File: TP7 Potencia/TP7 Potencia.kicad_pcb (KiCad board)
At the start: 2 copper layers, 55 parts, among them J1 Input, Q1 IRF830PBF, Q2 IRF830PBF, Q3 IRF830PBF, Q4 IRF830PBF, Q5 BC337, Q6 BC337, Q7 2N7000, Q8 2N7000, SW1 SW_Push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

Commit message: Placement de componentes en el PCB
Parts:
- added D11: MUR160, MUR160:DIOAD1300W80L670D310, F.Cu at (225.7, 34.5)
- added D12: MUR160, MUR160:DIOAD1300W80L670D310, F.Cu at (236.2, 49.7)
- added D13: MUR160, MUR160:DIOAD1300W80L670D310, F.Cu at (153.5, 50.2)
- added D14: MUR160, MUR160:DIOAD1300W80L670D310, F.Cu at (147.2, 39.6)
- added J2: PWM, Connector_PinSocket_2.54mm:PinSocket_1x01_P2.54mm_Vertical, F.Cu at (55.6, 26.9)
- moved U6 171.0 mm to (255.6, 145.2)
- moved C10 160.3 mm to (236.4, 144.0)
- moved C8 160.3 mm to (236.4, 137.7)
- moved C9 160.3 mm to (236.4, 140.8)
- moved D7 160.3 mm to (242.2, 118.7)
- moved D8 160.3 mm to (242.2, 122.2)
- moved D9 160.3 mm to (242.2, 125.8)
- moved Q5 160.3 mm to (230.3, 129.9)
- moved Q6 160.3 mm to (230.3, 135.7)
- moved Q7 160.3 mm to (230.3, 141.5)
- moved Q8 160.3 mm to (230.3, 147.3)
- moved RV3 160.3 mm to (269.8, 117.9)
- moved RV4 160.3 mm to (269.8, 124.0)
- moved R10 160.3 mm to (208.6, 121.8)
- moved R11 160.3 mm to (208.6, 125.8)
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
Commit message: Ordenados los componentes por bloques
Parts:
- D11, D12, D13, D14, D2, D4: footprint MUR160:DIOAD1300W80L670D310 -> Diode_THT:D_DO-35_SOD27_P7.62mm_Horizontal
- moved RV3 153.4 mm to (120.2, 83.8), turned to 90 degrees
- moved RV4 124.6 mm to (148.7, 94.8), turned to 90 degrees
- moved D9 105.9 mm to (141.0, 94.4), turned to -90 degrees
- moved U5 104.5 mm to (128.6, 84.5)
- moved D12 101.7 mm to (134.5, 50.4), turned to -90 degrees
- moved U6 99.2 mm to (232.6, 48.6)
- moved D11 97.7 mm to (128.3, 42.6), turned to -90 degrees
- moved R10 93.7 mm to (119.7, 92.1), turned to -90 degrees
- moved C10 89.6 mm to (156.8, 102.9), turned to -90 degrees
- moved Q5 87.5 mm to (155.9, 83.8), turned to -90 degrees
- moved R9 87.5 mm to (125.0, 91.9), turned to -90 degrees
- moved Q7 85.2 mm to (156.9, 98.3), turned to 90 degrees
- moved C8 82.5 mm to (219.8, 56.9)
- moved R12 81.8 mm to (140.1, 85.1)
- moved Q8 81.1 mm to (173.5, 89.4), turned to 90 degrees
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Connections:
- C1 pad 1: Net-(U2-VB) -> Net-(D2-K)
- C4 pad 1: Net-(U2-VB) -> Net-(D2-K)
- C5 pad 1: Net-(U3-VB) -> Net-(D4-K)
- C6 pad 1: Net-(U3-VB) -> Net-(D4-K)
- D10 pad 2: Net-(D10-A) -> SD
- Q8 pad 1: Net-(D10-A) -> SD
- R16 pad 2: Net-(D10-A) -> SD
- U2 pad 6: Net-(U2-VB) -> Net-(D2-K)
- U3 pad 6: Net-(U3-VB) -> Net-(D4-K)

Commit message: Ruteo
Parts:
- Q6: moved to B.Cu
- moved D8 182.4 mm to (58.9, 56.4), turned to 0 degrees
- moved R8 179.2 mm to (67.2, 51.2), turned to 180 degrees
- moved C9 178.5 mm to (55.7, 56.4)
- moved U6 174.3 mm to (59.1, 64.9), turned to 90 degrees
- moved R7 171.1 mm to (51.4, 77.7), turned to 0 degrees
- moved D7 165.9 mm to (60.1, 73.2), turned to 180 degrees
- moved C8 153.9 mm to (67.3, 77.7), turned to 90 degrees
- moved C4 76.7 mm to (177.1, 39.7), turned to 180 degrees
- moved D1 74.6 mm to (185.2, 41.7)
- moved D2 74.6 mm to (179.3, 36.3)
- moved R3 74.6 mm to (183.9, 37.2)
- moved C1 74.6 mm to (186.1, 46.6)
- moved D11 74.6 mm to (202.9, 44.3)
- moved Q1 74.6 mm to (195.8, 48.6)
- moved U2 74.6 mm to (179.7, 59.3)
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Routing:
- net 12V: track 0.00 -> 205.3 mm
- net H1: track 0.00 -> 57.8 mm
- net H2: track 0.00 -> 54.4 mm
- net PWM: track 0.00 -> 45.0 mm
- net H: track 0.00 -> 36.4 mm
- net Net-(D4-K): track 0.00 -> 19.4 mm
- net 5V: track 0.00 -> 18.9 mm
- net Net-(D2-K): track 0.00 -> 18.7 mm
- net Net-(U1-DTC): track 0.00 -> 17.3 mm
- net B: track 0.00 -> 16.7 mm
- net Net-(D3-A): track 0.00 -> 14.7 mm
- net Net-(D6-A): track 0.00 -> 13.9 mm
- net Net-(D6-K): track 0.00 -> 12.9 mm
- net E: track 0.00 -> 12.7 mm
- net Net-(D3-K): track 0.00 -> 11.6 mm
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
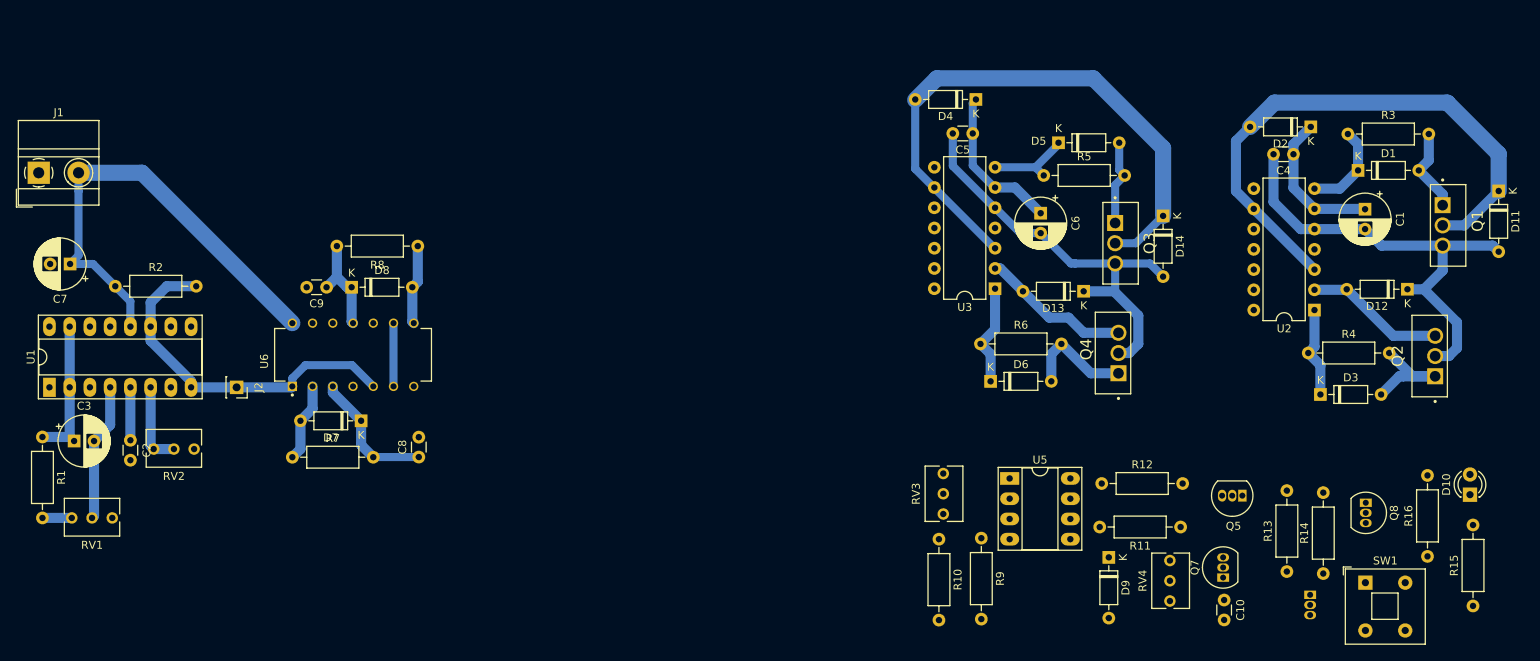
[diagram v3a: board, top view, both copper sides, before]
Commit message: continuacion del rooteo y agregado de testpoint y borneras
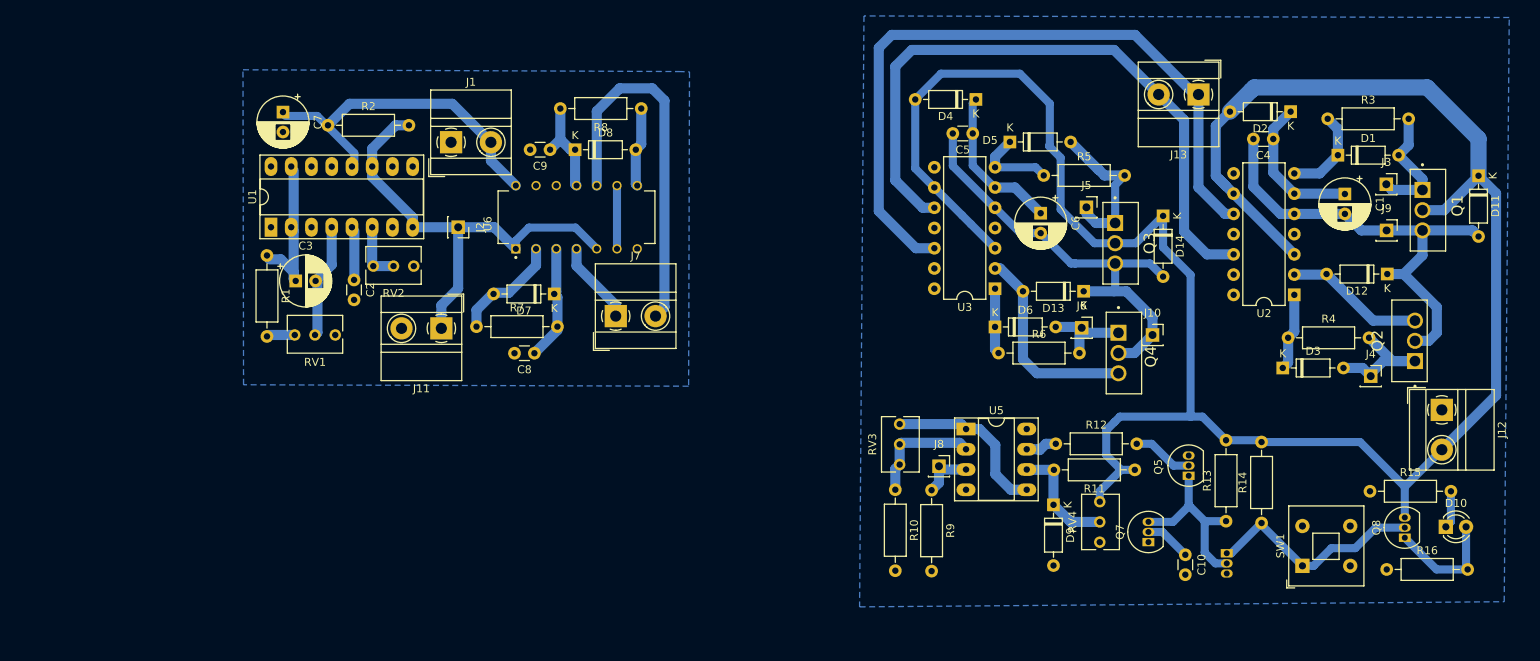
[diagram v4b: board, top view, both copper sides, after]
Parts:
- added J10: H2, Connector_PinSocket_2.54mm:PinSocket_1x01_P2.54mm_Vertical, F.Cu at (159.4, 62.4)
- added J11: GND/PWM, TerminalBlock_MetzConnect:TerminalBlock_MetzConnect_Type011_RT05502HBWC_1x02_P5.00mm_Horizontal, F.Cu at (70.1, 61.5)
- added J12: Input, TerminalBlock_MetzConnect:TerminalBlock_MetzConnect_Type011_RT05502HBWC_1x02_P5.00mm_Horizontal, F.Cu at (195.7, 71.8)
- added J13: PWM1/PWM2, TerminalBlock_MetzConnect:TerminalBlock_MetzConnect_Type011_RT05502HBWC_1x02_P5.00mm_Horizontal, F.Cu at (165.2, 32.2)
- added J3: Gate Q1, Connector_PinSocket_2.54mm:PinSocket_1x01_P2.54mm_Vertical, F.Cu at (188.8, 43.5)
- added J4: Gate Q2, Connector_PinSocket_2.54mm:PinSocket_1x01_P2.54mm_Vertical, F.Cu at (186.8, 67.5)
- added J5: Gate Q3, Connector_PinSocket_2.54mm:PinSocket_1x01_P2.54mm_Vertical, F.Cu at (151.1, 46.4)
- added J6: Gate Q4, Connector_PinSocket_2.54mm:PinSocket_1x01_P2.54mm_Vertical, F.Cu at (150.5, 61.5)
- added J7: Output, TerminalBlock_MetzConnect:TerminalBlock_MetzConnect_Type011_RT05502HBWC_1x02_P5.00mm_Horizontal, F.Cu at (92.0, 60.0)
- added J8: H, Connector_PinSocket_2.54mm:PinSocket_1x01_P2.54mm_Vertical, F.Cu at (132.6, 78.9)
- added J9: H1, Connector_PinSocket_2.54mm:PinSocket_1x01_P2.54mm_Vertical, F.Cu at (188.8, 49.3)
- moved J1 51.9 mm to (71.4, 38.2)
- moved R1 36.2 mm to (48.2, 52.4)
- moved RV1 36.2 mm to (51.7, 62.4)
- moved RV2 35.9 mm to (61.6, 53.7)
- moved C2 34.5 mm to (59.2, 55.5)
- moved C3 34.3 mm to (51.9, 55.6)
- moved J2 34.3 mm to (72.3, 48.9)
- moved U1 34.3 mm to (48.8, 48.9)
- moved R2 33.5 mm to (55.9, 36.1)
- moved C9 32.9 mm to (83.8, 39.1)
- moved D8 32.9 mm to (86.9, 39.1)
- moved R8 32.9 mm to (95.2, 34.0)
- moved U6 32.9 mm to (87.1, 47.6)
- moved C7 32.8 mm to (50.3, 34.4), turned to -90 degrees
- moved D7 29.0 mm to (84.3, 57.2)
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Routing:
- net PWM2: track 0.00 -> 130.0 mm
- net 12V: track 205.3 -> 317.9 mm
- net PWM1: track 0.00 -> 101.2 mm
- net Net-(Q6-C): track 0.00 -> 34.1 mm
- net Net-(Q5-C): track 0.00 -> 22.5 mm
- net Net-(U5B-+): track 0.00 -> 21.5 mm
- net SD: track 0.17 -> 15.0 mm
- net Net-(U5A--): track 0.00 -> 14.7 mm
- net Net-(D9-K): track 0.00 -> 14.5 mm
- net H: track 36.4 -> 50.5 mm
- net PWM: track 45.0 -> 58.4 mm
- net Net-(D5-A): track 10.9 -> 19.9 mm
- net Net-(Q5-B): track 0.00 -> 7.65 mm
- net Net-(D1-A): track 10.7 -> 15.5 mm
- net Net-(D7-A): track 9.94 -> 14.6 mm
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- added copper zone on B.Cu, net GND

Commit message: fin del rooteo
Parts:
- RV1: footprint Potentiometer_THT:Potentiometer_Bourns_3266Y_Vertical -> Potentiometer_THT:Potentiometer_Alps_RK163_Single_Horizontal
- moved R1 12.8 mm to (44.9, 40.0)
- moved J12 5.99 mm to (198.3, 77.2), turned to 90 degrees
- moved RV1 4.60 mm to (49.8, 66.5), turned to 90 degrees
- moved D7 3.14 mm to (87.4, 57.9)
- moved R7 2.67 mm to (77.2, 61.2)
- moved J11 2.51 mm to (72.7, 61.5)
- moved C7 2.10 mm to (50.3, 32.3)
- moved D2 1.19 mm to (177.8, 33.8)
- moved J10 1.19 mm to (160.5, 62.0)
- moved J6 0.27 mm to (150.5, 61.2)
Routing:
- net SD: track 15.0 -> 215.5 mm, vias 0 -> 6
- net H: track 50.5 -> 99.6 mm, vias 0 -> 2
- net Net-(U5B-+): track 21.5 -> 43.2 mm
- net Net-(R1-Pad2): track 3.56 -> 18.4 mm
- net 5V: track 17.7 -> 23.9 mm
- net 12V: track 317.9 -> 323.0 mm, vias 0 -> 4
- net B: track 14.6 -> 18.8 mm
- net Net-(U1-DTC): track 14.6 -> 18.7 mm
- net Net-(D7-A): track 14.6 -> 11.6 mm
- net H2: track 57.2 -> 59.2 mm
- net Net-(D2-K): track 18.7 -> 19.9 mm
- net PWM: track 58.4 -> 57.7 mm
- net Net-(D6-A): track 11.5 -> 12.1 mm

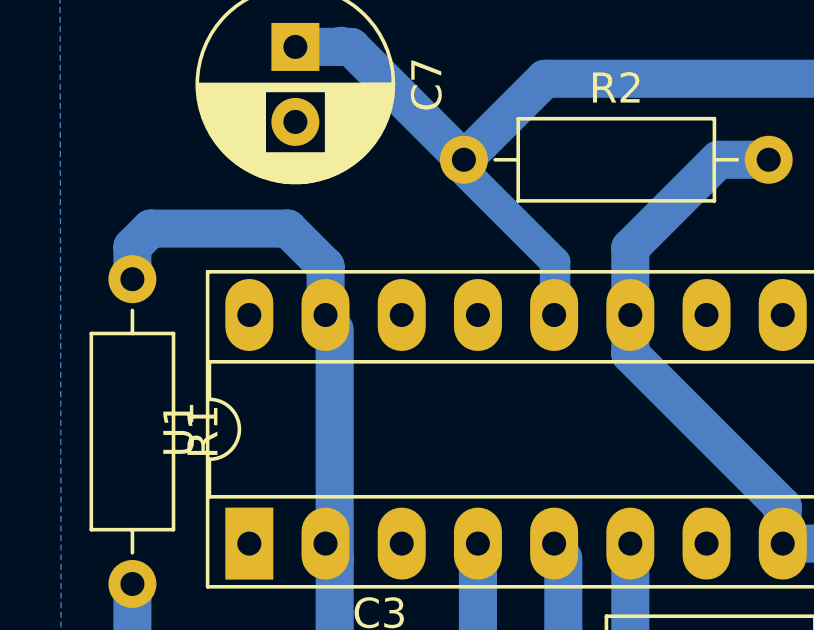
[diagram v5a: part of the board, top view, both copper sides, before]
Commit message: corrección del fin de rooteo
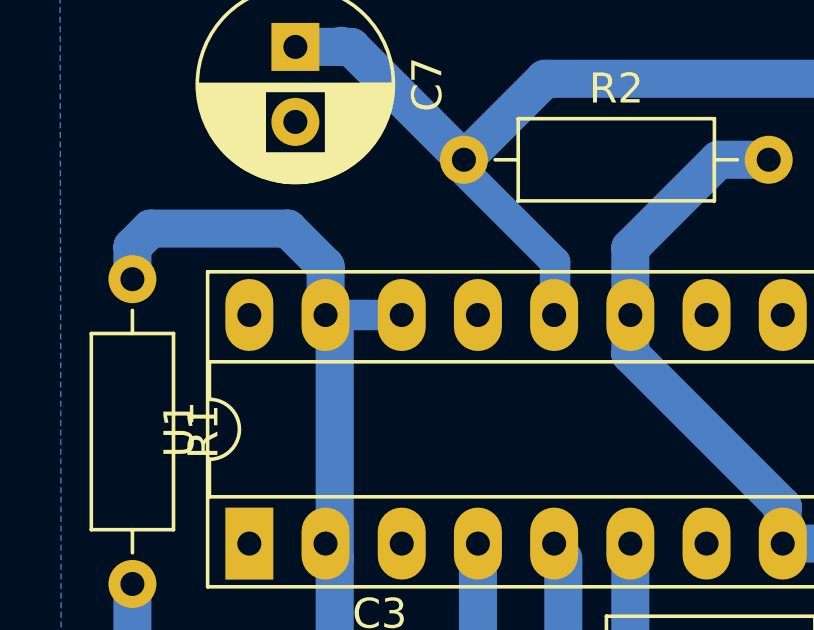
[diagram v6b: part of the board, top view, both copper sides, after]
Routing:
- net 5V: track 23.9 -> 26.4 mm
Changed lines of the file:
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@@
   (segment (start 51.297 39.613) (end 51.297 41.234) (width 1.27) (layer "B.Cu") (net 5))
   (segment (start 51.602 54.495) (end 51.602 55.342) (width 1.27) (layer "B.Cu") (net 5))
+  (segment (start 51.297 41.234) (end 53.837 41.234) (width 1.016) (layer "B.Cu") (net 5))
   (segment (start 51.602 55.342) (end 51.855 55.595) (width 1.27) (layer "B.Cu") (net 5))
   (segment (start 54.784 66.548) (end 54.784 56.024) (width 1.27) (layer "B.Cu") (net 6))
